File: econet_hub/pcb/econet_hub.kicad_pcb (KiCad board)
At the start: 2 copper layers, 70.7 x 36.6 mm, 22 parts

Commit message: econet_hub is ready to go
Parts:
- removed the EXTPWR at (95.3, 94.5)
- added EXTPWR: ext pwr, Pin_Headers:Pin_Header_Straight_2x03_Pitch2.54mm, F.Cu at (99.3, 97.9)
- added USB: usb, myelin-kicad:micro_usb_b_smd_molex, F.Cu at (91.2, 87.3)
- added staple_single5: , myelin-kicad:via_single, F.Cu at (95.6, 88.6)
- moved staple_single3 21.4 mm to (97.0, 83.8)
- moved C2 7.97 mm to (98.1, 89.9), turned to 0 degrees
- moved C1 1.70 mm to (114.4, 91.3)
- moved ISP 1.70 mm to (105.2, 92.8)
- moved staple_single4 1.70 mm to (116.3, 92.5)
- moved AVR 1.70 mm to (114.3, 95.3)
- moved R1 1.70 mm to (114.3, 99.3)
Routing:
- net 5V: track 16.0 -> 44.2 mm
- net econet_clock_line_P: track 87.6 -> 99.2 mm
- net econet_clock_line_M: track 96.7 -> 104.2 mm
- net GND: track 72.2 -> 76.7 mm
- net econet_data_line_M: track 89.8 -> 91.0 mm
- net avr_MISO: track 7.76 -> 7.19 mm
- added copper zone on F.Cu, net GND
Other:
- board text added: "1"
- board text added: "5V x 3"
- board text added: "Econet Hub Phillip Pearson 2017 http://myelin.nz/acorn/ecohub"
- board text added: "Econet Hub Phillip Pearson 2017 http://myelin.nz/acorn/ecohub Copyright 2017 Google LLC"
- board text added: "GND x 3"

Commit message: econet_hub changes from months ago; finally fixed the bad ATTINY85 footprint and added some more docs
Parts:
- removed the AVR at (114.3, 95.3)
- added AVR: ATTINY85-20SU, Housings_SOIC:SOIJ-8_5.3x5.3mm_Pitch1.27mm, F.Cu at (114.3, 95.3)
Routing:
- net 5V: track 44.2 -> 46.0 mm
- net avr_SCK: track 7.23 -> 6.27 mm
- net econet_clock_line_M: track 104.2 -> 103.3 mm
- net avr_MISO: track 7.19 -> 6.28 mm
- net econet_clock_line_P: track 99.2 -> 98.6 mm
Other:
- board text added: "Econet Hub r2 Phillip Pearson 2017 http://myelin.nz/acorn/ecohub"
- board text added: "Econet Hub r2 Phillip Pearson 2017 http://myelin.nz/acorn/ecohub Copyright 2017 Google LLC"
- board text added: "TODO add room around attiny85 in case it needs resoldering TODO add barrel jack maybe? TODO is there room for another two sockets? TODO mounting holes"
- board text removed: "Econet Hub Phillip Pearson 2017 http://myelin.nz/acorn/ecohub"
- board text removed: "Econet Hub Phillip Pearson 2017 http://myelin.nz/acorn/ecohub Copyright 2017 Google LLC"

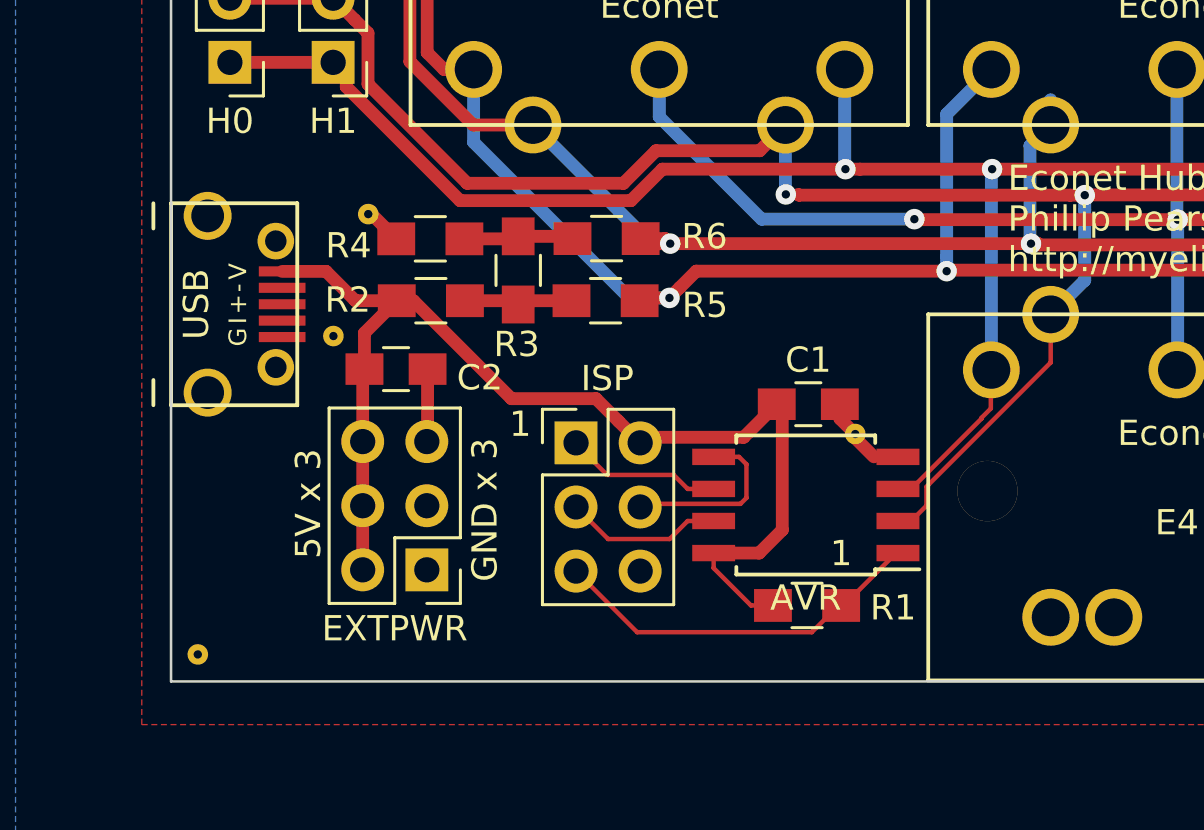
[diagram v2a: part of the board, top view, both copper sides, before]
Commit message: Added room around ATTINY85
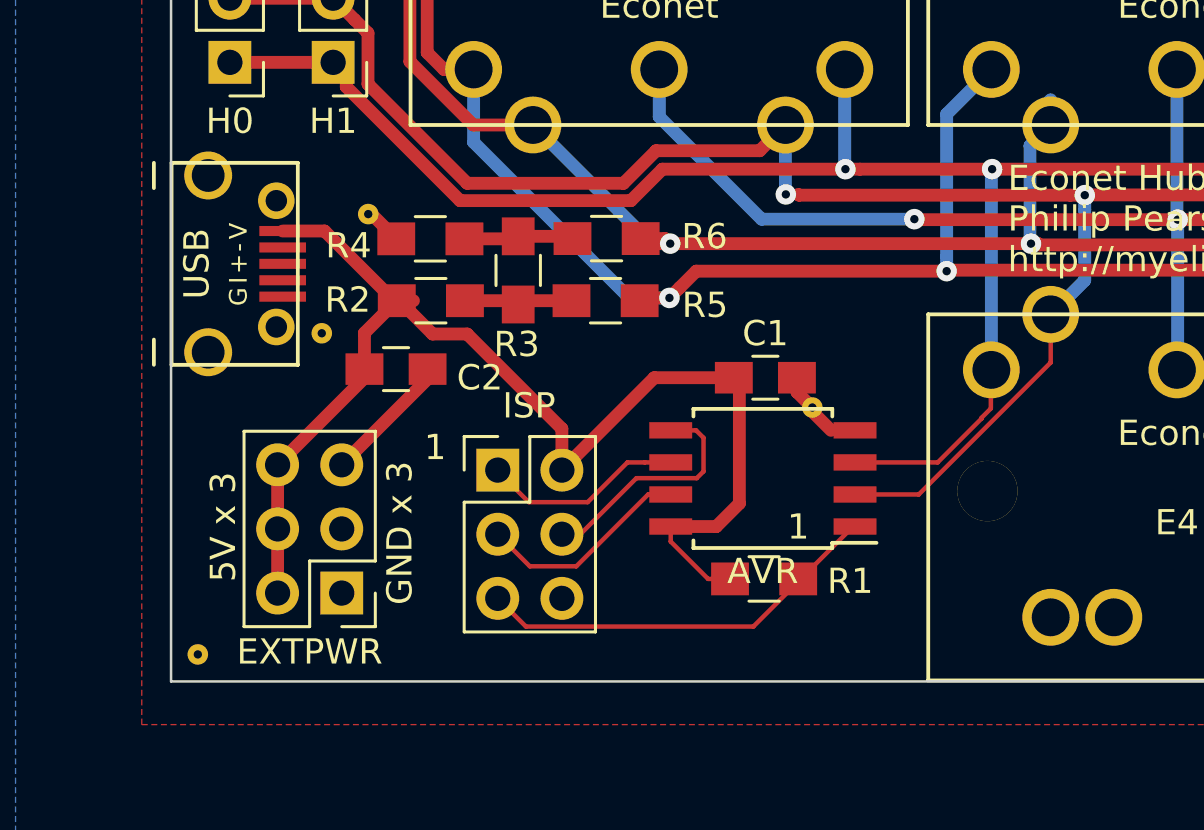
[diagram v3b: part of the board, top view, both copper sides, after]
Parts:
- moved EXTPWR 3.49 mm to (95.9, 98.8)
- moved ISP 3.28 mm to (102.1, 93.9)
- moved AVR 2.00 mm to (112.6, 94.2)
- moved C1 2.00 mm to (112.7, 90.3)
- moved staple_single4 2.00 mm to (114.6, 91.4)
- moved R1 2.00 mm to (112.7, 98.2)
- moved USB 1.60 mm to (91.2, 85.8)
- moved staple_single5 0.47 mm to (95.1, 88.5)
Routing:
- net 5V: track 46.0 -> 50.6 mm
- net avr_MOSI: track 7.13 -> 9.55 mm
- net GND: track 76.7 -> 79.1 mm
- net avr_SCK: track 6.27 -> 8.55 mm
- net avr_MISO: track 6.28 -> 8.10 mm
- net econet_clock_line_M: track 103.3 -> 105.1 mm
- net econet_clock_line_P: track 98.6 -> 100.0 mm
- net avr_nRESET: track 15.1 -> 16.3 mm
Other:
- board text added: "TODO add barrel jack maybe? TODO is there room for another two sockets? TODO mounting holes"
- board text removed: "TODO add room around attiny85 in case it needs resoldering TODO add barrel jack maybe? TODO is there room for another two sockets? TODO mounting holes"

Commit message: econet hub v2
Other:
- board text added: "C- C+ 0 D- D+"
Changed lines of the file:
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@@
   (general
     (thickness 1.6)
-    (drawings 11)
+    (drawings 12)
     (tracks 239)
     (zones 0)
@@
     (descr "Through hole straight pin header, 2x03, 2.54mm pitch, double rows")
     (tags "Through hole pin header THT 2x03 2.54mm double row")
-    (fp_text reference ISP (at 1.24 -2.55) (layer F.SilkS)
+    (fp_text reference ISP (at 1.17 7.64) (layer F.SilkS)
       (effects (font (size 1 1) (thickness 0.15)))
     )
@@
     (tags "resistor 0805")
     (attr smd)
-    (fp_text reference R3 (at -2.93 -0.06 180) (layer F.SilkS)
+    (fp_text reference R3 (at 3.13 -0.16 180) (layer F.SilkS)
       (effects (font (size 1 1) (thickness 0.15)))
     )
@@
     (descr "Through hole straight pin header, 2x03, 2.54mm pitch, double rows")
     (tags "Through hole pin header THT 2x03 2.54mm double row")
-    (fp_text reference EXTPWR (at 1.27 -2.33 180) (layer F.SilkS)
+    (fp_text reference EXTPWR (at 1.2 -2.68 180) (layer F.SilkS)
       (effects (font (size 1 1) (thickness 0.15)))
     )
@@
     (tags "SOIC 1.27")
     (attr smd)
-    (fp_text reference AVR (at 0 -3.68 180) (layer F.SilkS)
+    (fp_text reference AVR (at 4.02 3.92 180) (layer F.SilkS)
       (effects (font (size 1 1) (thickness 0.15)))
     )
@@
     )
   )
+  (gr_text "C- C+ 0 D- D+" (at 93.53 72.72 90) (layer F.SilkS)
+    (effects (font (size 1 1) (thickness 0.2)))
+  )
   (gr_text "TODO add barrel jack maybe?\nTODO is there room for another two sockets?\nTODO mounting holes" (at 103.68 107.37) (layer Eco2.User)
     (effects (font (size 1 1) (thickness 0.2)) (justify left))
@@
     (effects (font (size 1 1) (thickness 0.2)))
   )
-  (gr_text 1 (at 114 96.17) (layer F.SilkS)
+  (gr_text 1 (at 118.17 96.4) (layer F.SilkS)
     (effects (font (size 1 1) (thickness 0.2)))
   )
